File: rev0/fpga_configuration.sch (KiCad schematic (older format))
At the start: 0 parts

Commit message: schematic: capture additional... capture
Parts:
- added C? (x5): 0.1uF, symbol Device:C
- added IC?: ECP5-BGA256, BGA256C80P16X16_1400X1400X170, symbol fpgas_and_processors:ECP5-BGA256
- added R? (x3): R, symbol Device:R
- added U?: ATSAMD21G18A-AUT, Package_QFP:TQFP-48_7x7mm_P0.5mm, symbol MCU_Microchip_SAMD:ATSAMD21G18A-AUT
- added U?: W25Q32JVSS, Package_SO:SOIC-8_5.23x5.23mm_P1.27mm, symbol Memory_Flash:W25Q32JVSS
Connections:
- net labels added: +3V3, CONFIG_UC_RESET, D0, D1, D2, D3, GND, SPI_CLK, ~CS
- wire segments 0 -> 54
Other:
- note added: "By default, select MSPI \nmode, so the ECP5 will \nself-configure from flash."
- note added: "Development / Debug uC"
- note added: "replace w/ ATSAMD21G15B (smaller flash) in later rev"

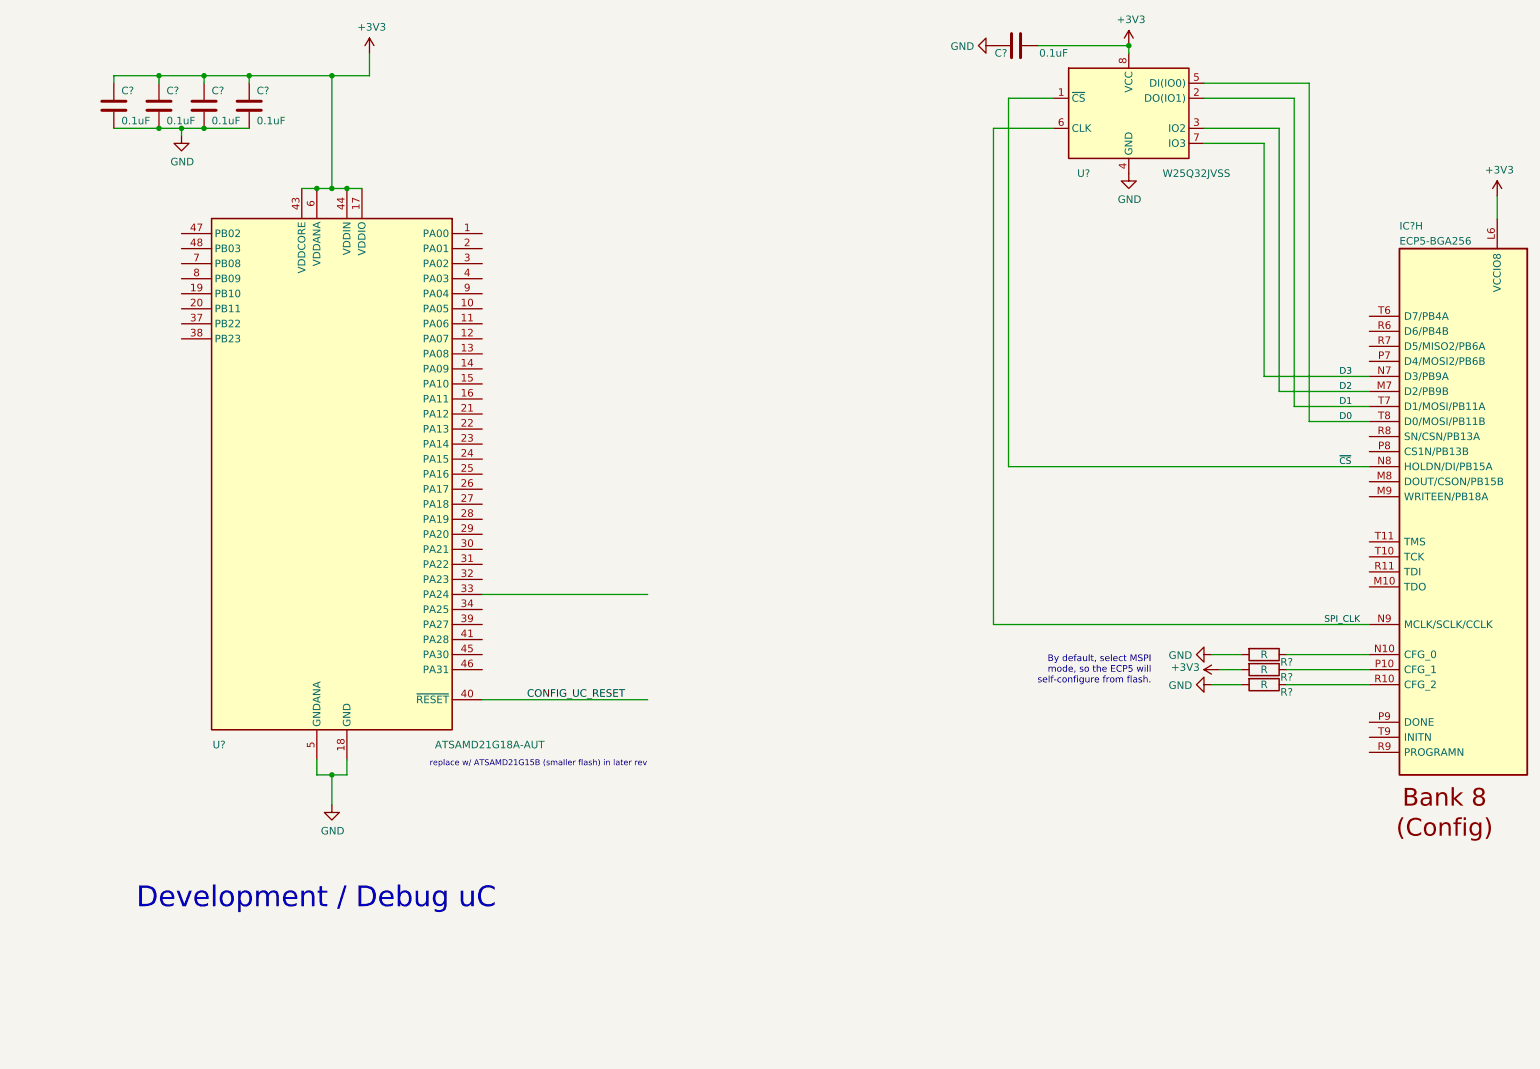
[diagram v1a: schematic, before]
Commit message: schematic: complete initial configuration section
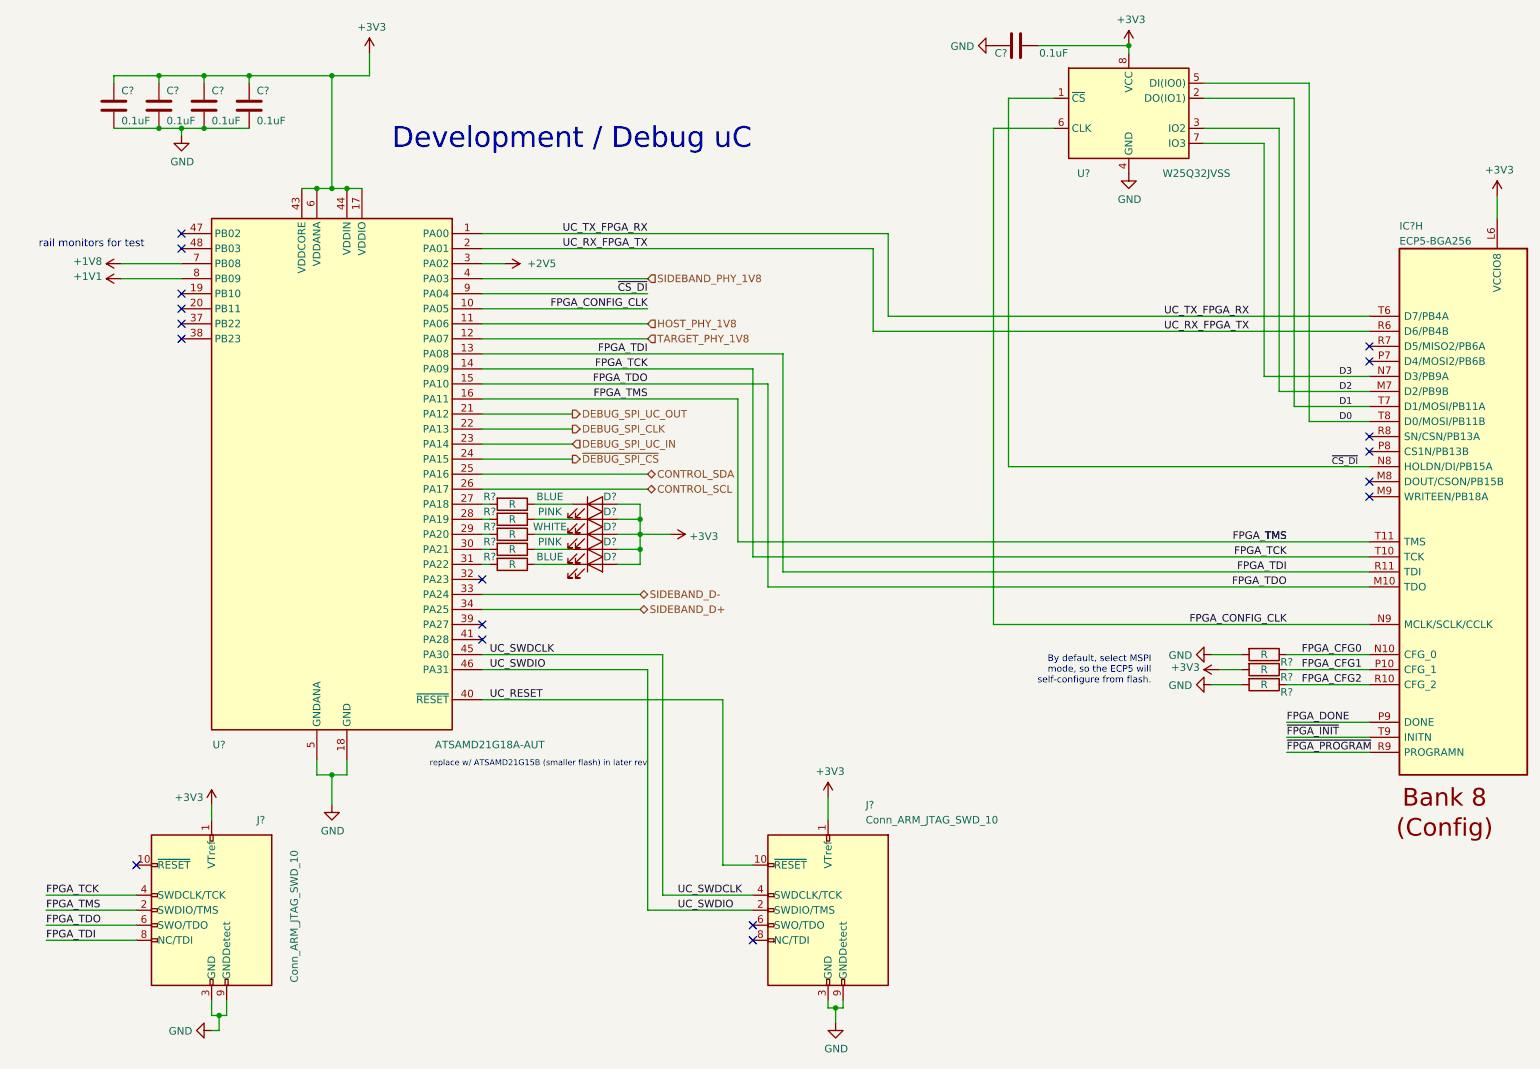
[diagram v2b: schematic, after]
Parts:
- added D? (x2): BLUE, symbol Device:LED
- added D? (x2): PINK, symbol Device:LED
- added D?: WHITE, symbol Device:LED
- added J? (x2): Conn_ARM_JTAG_SWD_10, symbol Connector:Conn_ARM_JTAG_SWD_10
- added R? (x5): R, symbol Device:R
- gave numbers to parts that had none: 11
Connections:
- net labels added: +1V1, +1V8, +2V5, CONTROL_SCL, CONTROL_SDA, DEBUG_SPI_CLK, DEBUG_SPI_UC_IN, DEBUG_SPI_UC_OUT, FPGA_CFG0, FPGA_CFG1, FPGA_CFG2, FPGA_CONFIG_CLK, FPGA_DONE, FPGA_TCK, FPGA_TDI, FPGA_TDO, FPGA_TMS, HOST_PHY_1V8, SIDEBAND_D+, SIDEBAND_D-, SIDEBAND_PHY_1V8, TARGET_PHY_1V8, TMS, UC_RESET, UC_RX_FPGA_TX, UC_SWDCLK, UC_SWDIO, UC_TX_FPGA_RX, ~CS_DI, ~DEBUG_SPI_CS, ~FPGA_INIT, ~FPGA_PROGRAM
- net labels removed: CONFIG_UC_RESET, SPI_CLK, ~CS
- wire segments 54 -> 135
- no-connect marks 0 -> 18
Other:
- note added: "rail monitors for test"

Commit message: schematic: capture host section
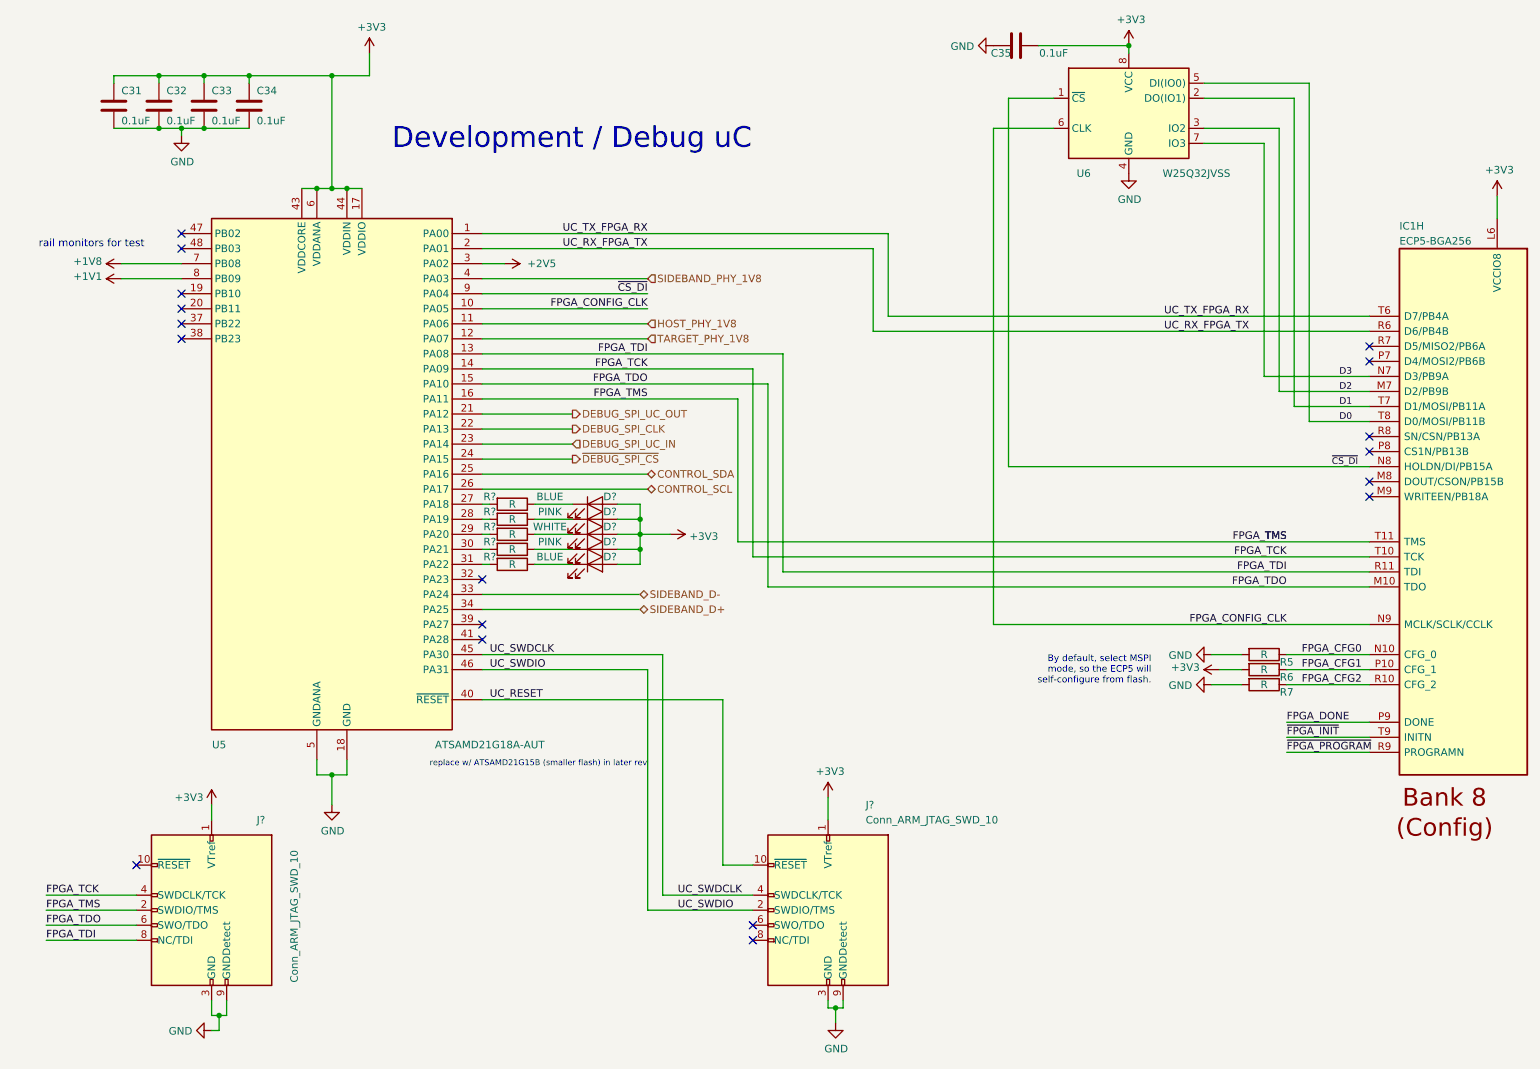
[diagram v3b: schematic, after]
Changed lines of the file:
@@
 $Descr A4 11693 8268
 encoding utf-8
-Sheet 3 3
+Sheet 3 5
 Title "LUNA USB Multitool"
 Date "2019-10-16"
@@
 U 8 1 5DCABD39
 P 10500 2250
-F 0 "IC?" H 11350 2400 50  0000 R CNN
+F 0 "IC1" H 11350 2400 50  0000 R CNN
 F 1 "ECP5-BGA256" H 11350 2300 50  0000 R CNN
 F 2 "BGA256C80P16X16_1400X1400X170" H 7300 5700 50  0001 L CNN
@@
 U 1 1 5DCDEED8
 P 10300 1900
-F 0 "#PWR?" H 10300 1750 50  0001 C CNN
+F 0 "#PWR0128" H 10300 1750 50  0001 C CNN
 F 1 "+3V3" H 10315 2073 50  0000 C CNN
 F 2 "" H 10300 1900 50  0001 C CNN
@@
 U 1 1 5DCEC8F9
 P 1400 1300
-F 0 "C?" H 1450 1400 50  0000 L CNN
+F 0 "C32" H 1450 1400 50  0000 L CNN
 F 1 "0.1uF" H 1450 1200 50  0000 L CNN
 F 2 "" H 1438 1150 50  0001 C CNN
@@
 U 1 1 5DCEDCE6
 P 1700 1300
-F 0 "C?" H 1750 1400 50  0000 L CNN
+F 0 "C33" H 1750 1400 50  0000 L CNN
 F 1 "0.1uF" H 1750 1200 50  0000 L CNN
 F 2 "" H 1738 1150 50  0001 C CNN
@@
 U 1 1 5DCEE41C
 P 2000 1300
-F 0 "C?" H 2050 1400 50  0000 L CNN
+F 0 "C34" H 2050 1400 50  0000 L CNN
 F 1 "0.1uF" H 2050 1200 50  0000 L CNN
 F 2 "" H 2038 1150 50  0001 C CNN
@@
 U 1 1 5DCEE96F
 P 1100 1300
-F 0 "C?" H 1150 1400 50  0000 L CNN
+F 0 "C31" H 1150 1400 50  0000 L CNN
 F 1 "0.1uF" H 1150 1200 50  0000 L CNN
 F 2 "" H 1138 1150 50  0001 C CNN
@@
 U 1 1 5DCEFFC7
 P 1550 1500
-F 0 "#PWR?" H 1550 1250 50  0001 C CNN
+F 0 "#PWR0129" H 1550 1250 50  0001 C CNN
 F 1 "GND" H 1555 1327 50  0000 C CNN
 F 2 "" H 1550 1500 50  0001 C CNN
@@
 U 1 1 5DD07968
 P 2800 950
-F 0 "#PWR?" H 2800 800 50  0001 C CNN
+F 0 "#PWR0130" H 2800 800 50  0001 C CNN
 F 1 "+3V3" H 2815 1123 50  0000 C CNN
 F 2 "" H 2800 950 50  0001 C CNN
@@
 U 1 1 5DD0C578
 P 2550 5950
-F 0 "#PWR?" H 2550 5700 50  0001 C CNN
+F 0 "#PWR0131" H 2550 5700 50  0001 C CNN
 F 1 "GND" H 2555 5777 50  0000 C CNN
 F 2 "" H 2550 5950 50  0001 C CNN
@@
 U 1 1 5DD128B2
 P 7850 1350
-F 0 "U?" H 7550 950 50  0000 C CNN
+F 0 "U6" H 7550 950 50  0000 C CNN
 F 1 "W25Q32JVSS" H 8300 950 50  0000 C CNN
 F 2 "Package_SO:SOIC-8_5.23x5.23mm_P1.27mm" H 7850 1350 50  0001 C CNN
@@
 U 1 1 5DD1D655
 P 7850 900
-F 0 "#PWR?" H 7850 750 50  0001 C CNN
+F 0 "#PWR0132" H 7850 750 50  0001 C CNN
 F 1 "+3V3" H 7865 1073 50  0000 C CNN
 F 2 "" H 7850 900 50  0001 C CNN
@@
 U 1 1 5DD1E101
 P 7850 1750
-F 0 "#PWR?" H 7850 1500 50  0001 C CNN
+F 0 "#PWR0133" H 7850 1500 50  0001 C CNN
 F 1 "GND" H 7855 1577 50  0000 C CNN
 F 2 "" H 7850 1750 50  0001 C CNN
@@
 U 1 1 5DD1E9FF
 P 7100 900
-F 0 "C?" V 7150 800 50  0000 C CNN
+F 0 "C35" V 7150 800 50  0000 C CNN
 F 1 "0.1uF" V 7150 1150 50  0000 C CNN
 F 2 "" H 7138 750 50  0001 C CNN
@@
 U 1 1 5DD21DA8
 P 6950 900
-F 0 "#PWR?" H 6950 650 50  0001 C CNN
+F 0 "#PWR0134" H 6950 650 50  0001 C CNN
 F 1 "GND" V 6955 772 50  0000 R CNN
 F 2 "" H 6950 900 50  0001 C CNN
@@
 U 1 1 5DD22BB5
 P 8750 4950
-F 0 "R?" V 8800 5100 50  0000 C CNN
+F 0 "R5" V 8800 5100 50  0000 C CNN
 F 1 "R" V 8750 4950 50  0000 C CNN
 F 2 "" V 8680 4950 50  0001 C CNN
@@
 U 1 1 5DD23434
 P 8750 5050
-F 0 "R?" V 8800 5200 50  0000 C CNN
+F 0 "R6" V 8800 5200 50  0000 C CNN
 F 1 "R" V 8750 5050 50  0000 C CNN
 F 2 "" V 8680 5050 50  0001 C CNN
@@
 U 1 1 5DD23797
 P 8750 5150
-F 0 "R?" V 8800 5300 50  0000 C CNN
+F 0 "R7" V 8800 5300 50  0000 C CNN
 F 1 "R" V 8750 5150 50  0000 C CNN
 F 2 "" V 8680 5150 50  0001 C CNN
@@
 U 1 1 5DD27B73
 P 8450 5050
-F 0 "#PWR?" H 8450 4900 50  0001 C CNN
+F 0 "#PWR0135" H 8450 4900 50  0001 C CNN
 F 1 "+3V3" V 8465 5178 50  0000 L CNN
 F 2 "" H 8450 5050 50  0001 C CNN
@@
 U 1 1 5DD2CC69
 P 8400 4950
-F 0 "#PWR?" H 8400 4700 50  0001 C CNN
+F 0 "#PWR0136" H 8400 4700 50  0001 C CNN
 F 1 "GND" V 8405 4822 50  0000 R CNN
 F 2 "" H 8400 4950 50  0001 C CNN
@@
 U 1 1 5DD2DED3
 P 8400 5150
-F 0 "#PWR?" H 8400 4900 50  0001 C CNN
+F 0 "#PWR0137" H 8400 4900 50  0001 C CNN
 F 1 "GND" V 8405 5022 50  0000 R CNN
 F 2 "" H 8400 5150 50  0001 C CNN
@@
 U 1 1 5DCDF84F
 P 2550 3750
-F 0 "U?" H 3300 1950 50  0000 C CNN
+F 0 "U5" H 3300 1950 50  0000 C CNN
 F 1 "ATSAMD21G18A-AUT" H 1500 1950 50  0000 C CNN
 F 2 "Package_QFP:TQFP-48_7x7mm_P0.5mm" H 1600 2000 50  0001 C CNN
